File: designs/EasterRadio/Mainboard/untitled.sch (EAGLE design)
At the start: 67 parts, among them IC1 74HC595D, IC2 74HC595D, IC3 74HC595D, IC4 Analog Digital

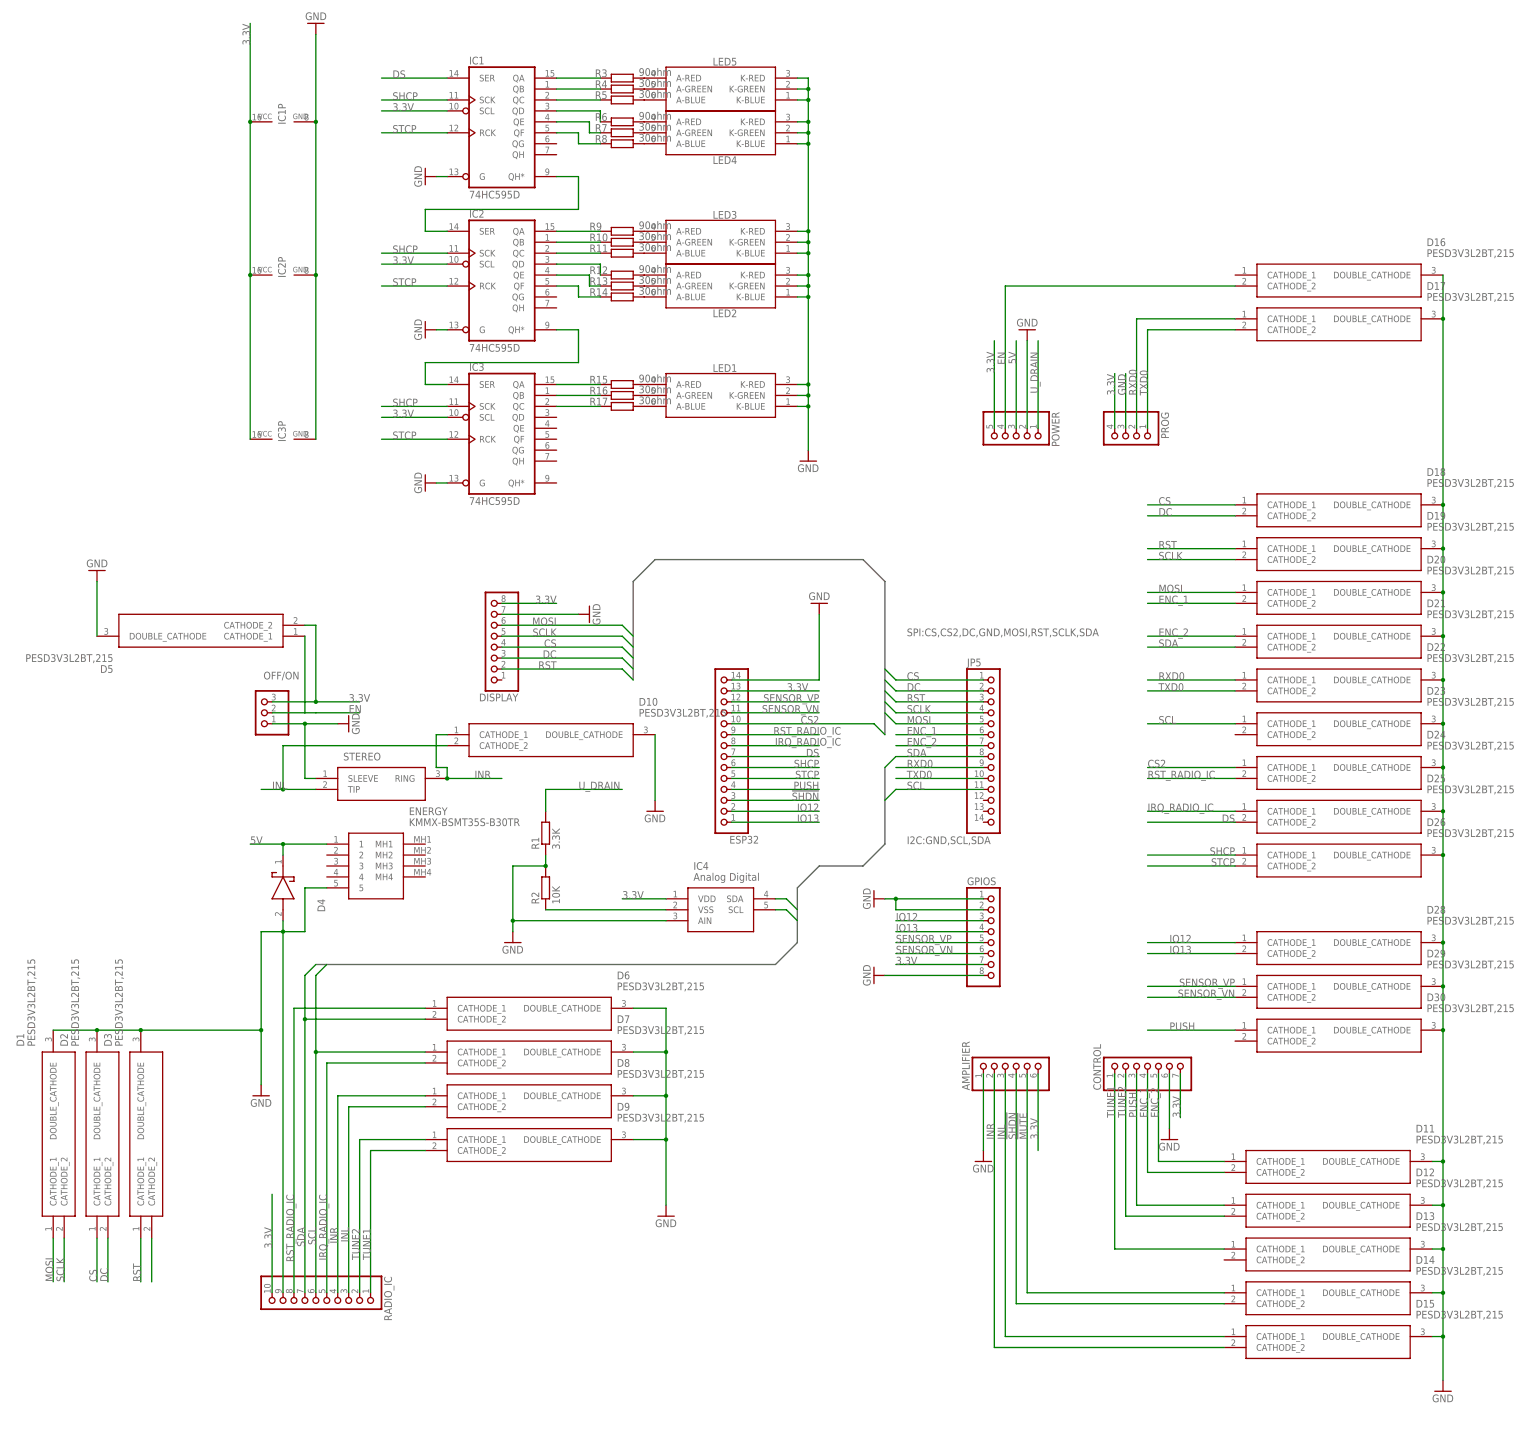
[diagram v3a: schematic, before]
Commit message: added new design of radio parts added 3.3V mark
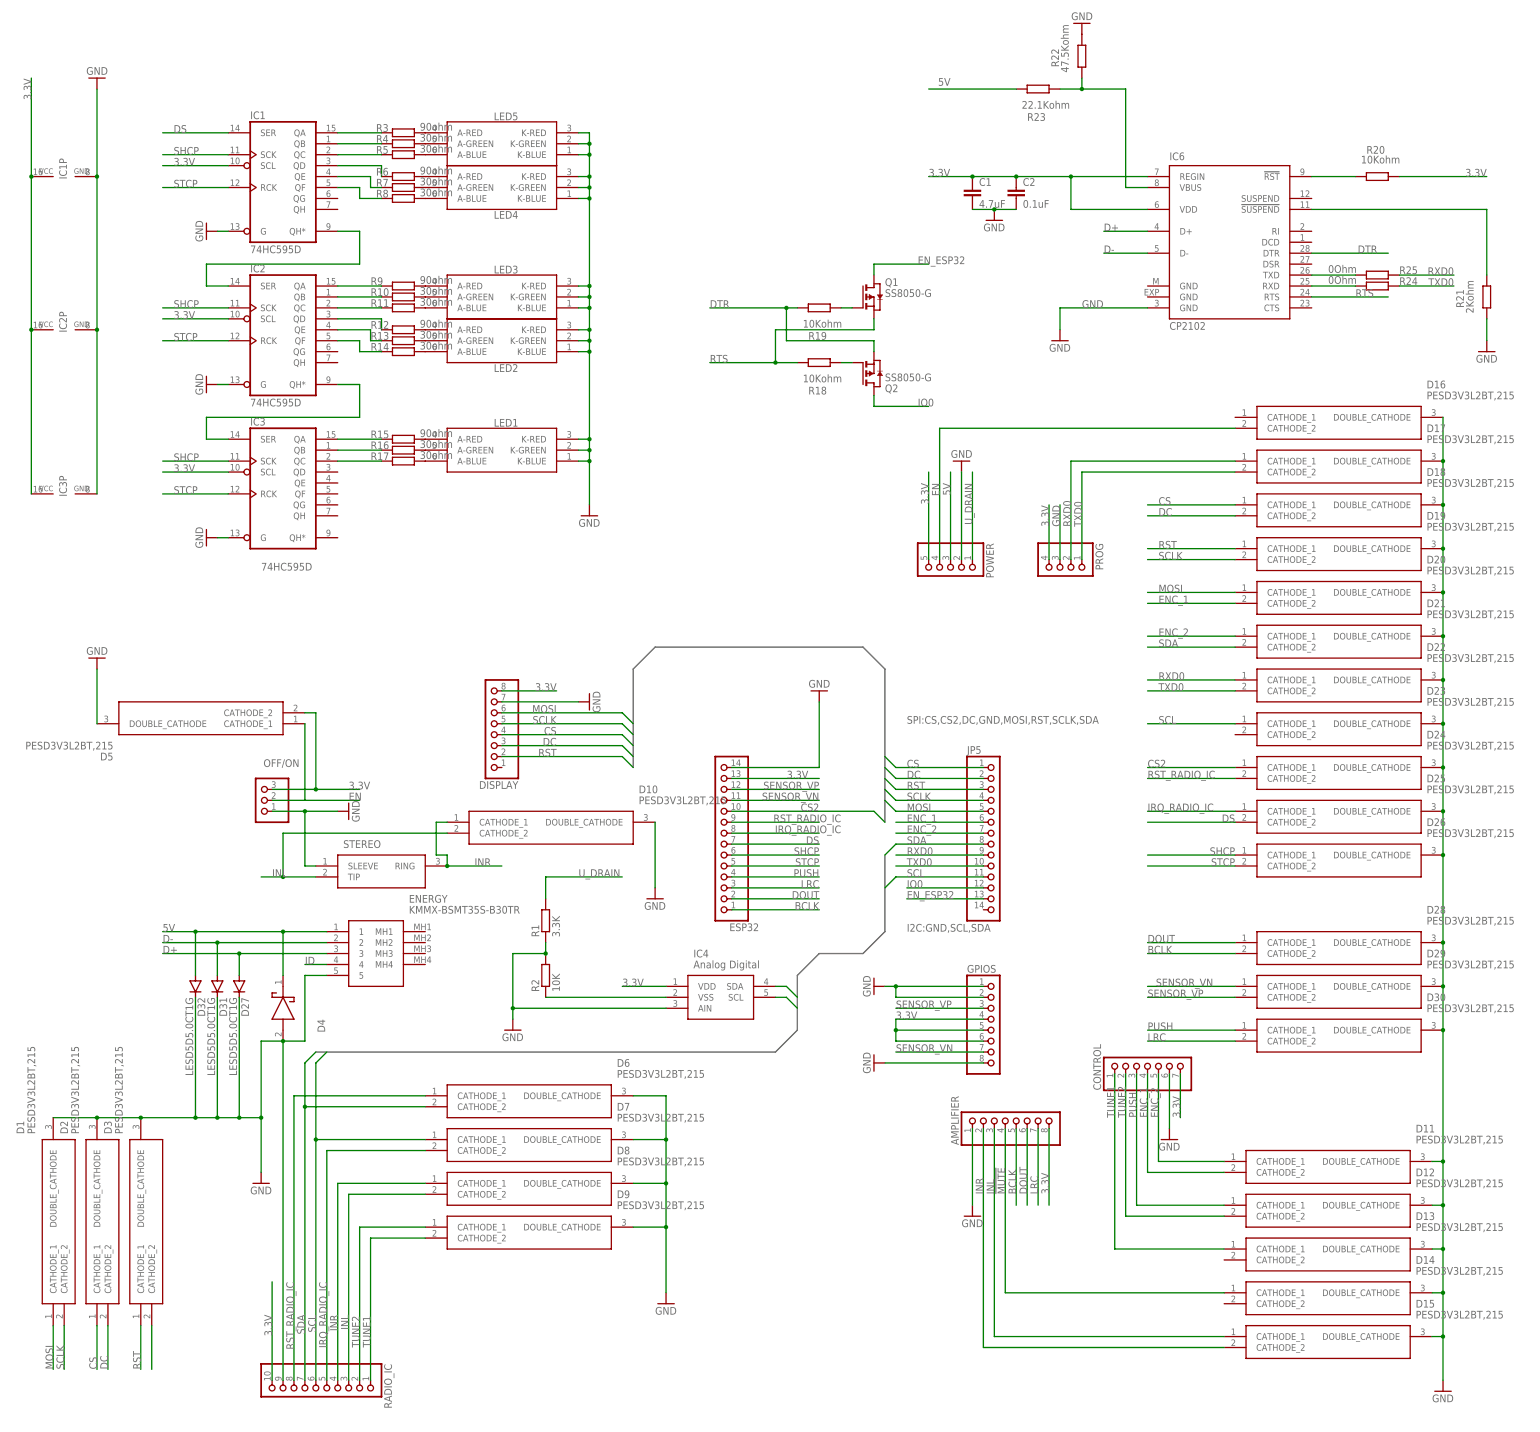
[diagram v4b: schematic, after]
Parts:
- added C1: 4.7uF, rcl:C-EUC0805
- added C2: 0.1uF, rcl:C-EUC0805
- added D27, D31, D32: LESD5D5.0CT1G, diode:DIODE-SOD523
- added IC6: CP2102, silabs:CP2102
- added Q1, Q2: SS8050-G, zetex:PMOSSOT23
- added R18, R19, R20: 10Kohm, rcl:R-EU_R0402
- added R21: 2Kohm, rcl:R-EU_R0805
- added R22: 47.5Kohm, rcl:R-EU_R0402
- added R23: 22.1Kohm, rcl:R-EU_R0402
- added R24, R25: 0Ohm, rcl:R-EU_R0603
- AMPLIFIER: device pinhead:PINHD-1X6 -> pinhead:PINHD-1X8
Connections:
- removed net !SHDN: AMPLIFIER.4, D14.CATHODE_2, ESP32.3
- removed net IO12: D28.CATHODE_1, ESP32.2, GPIOS.3
- removed net IO13: D28.CATHODE_2, ESP32.1, GPIOS.4
- new net BCLK: AMPLIFIER.5, D28.CATHODE_2, ESP32.1
- new net D+: D27.A, ENERGY.3, IC6.D+
- new net D-: D31.A, ENERGY.2, IC6.D-
- new net DOUT: AMPLIFIER.6, D28.CATHODE_1, ESP32.2
- new net DTR: IC6.DTR, Q2.S, R19.1
- new net EN_ESP32: JP5.13, Q1.D
- new net ID: ENERGY.4
- new net IO0: JP5.12, Q2.D
- new net LRC: AMPLIFIER.7, D30.CATHODE_2, ESP32.3
- new net N$1: Q2.G, R18.2
- new net N$2: Q1.G, R19.2
- new net N$38: IC6.!RST, R20.1
- new net N$43: IC6.!SUSPEND, R21.2
- new net N$44: IC6.VBUS, R22.1, R23.2
- new net N$45: IC6.TXD, R24.1
- new net N$46: IC6.RXD, R25.1
- new net RTS: IC6.RTS, Q1.S, R18.1
- net !MUTE: now also AMPLIFIER.4; no longer AMPLIFIER.5
- net 3.3V: now also AMPLIFIER.8, C1.1, C2.1, GPIOS.4, GPIOS.5, GPIOS.6, IC6.REGIN, IC6.VDD, R20.2; no longer AMPLIFIER.6, GPIOS.7
- net 5V: now also D32.A, R23.1
- net GND: now also C1.2, C2.2, D27.C, D31.C, D32.C, IC6.GND, R21.1, R22.2
- net RXD0: now also R24.2
- net SENSOR_VN: now also D29.CATHODE_1, GPIOS.7; no longer D29.CATHODE_2, GPIOS.6
- net SENSOR_VP: now also D29.CATHODE_2, GPIOS.3; no longer D29.CATHODE_1, GPIOS.5
- net TXD0: now also R25.2
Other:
- moved on the sheet: D1, D10, D16, D17, D2, D3, D4, D5, D6, D7, D8, D9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
